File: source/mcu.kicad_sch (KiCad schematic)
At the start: 31 parts, among them J4 TYPE-C-31-M-12, P13 SWD, SW2 SW_DPDT_x2, U11 STM32F401CCU6_Blackpill, U12 STM32F401CCU6_Blackpill, U13 STM32F405RGT6, Y1 8MHz Crystal Resonator, X5032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

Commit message: jlcpcb order
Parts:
- U14: renamed from U13; LCSC (none) -> C15742
- renumbered C61 to C72, C62 to C73, C63 to C74, C64 to C75, C65 to C76, C66 to C77, C67 to C78, C68 to C79, C69 to C80, C70 to C81, C71 to C82, C72 to C83, C73 to C84, C74 to C85, R60 to R62, R61 to R63, R62 to R64, R63 to R65, R64 to R66, U11 to U12, U12 to U13
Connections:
- net PA7: now reaches U13.16 (PB2)
- net PA7: now also U14.23 (PA7(ADC12_IN7))
- net PA6: now reaches U13.17 (PB10)
- net PA6: now also U14.22 (PA6(ADC12_IN6))
- net PA4: now reaches U13.28 (PA11)
- net PA4: now also U14.20 (PA4(ADC12_IN4/DAC1_OUT))
- net PA5: now reaches U13.29 (PA12)
- net PA5: now also U14.21 (PA5(ADC12_IN5/DAC2_OUT))
- net PC4: now reaches U13.30 (PA15)
- net PC4: now also U14.24 (PC4(ADC12_IN14))
- net PC5: now reaches U13.31 (PB3)
- net PC5: now also U14.25 (PC5(ADC12_IN15))
- net PD2: now reaches U13.32 (PB4)
- net PD2: now also U14.54 (PD2)
- net PB3: now reaches U13.33 (PB5)
- net PB3: now also U14.55 (PB3(JTDO/TRACESWO))
- net PB4: now reaches U13.34 (PB6)
- net PB4: now also U14.56 (PB4(NJTRST))
- net PB12: now reaches U13.35 (PB7)
- net PB12: now also U14.33 (PB12)
- net PB2: now reaches U14.28 (PB2-BOOT1)
- net PA15: now reaches U14.50 (PA15(JTDI))
- no-connect marks 52 -> 30

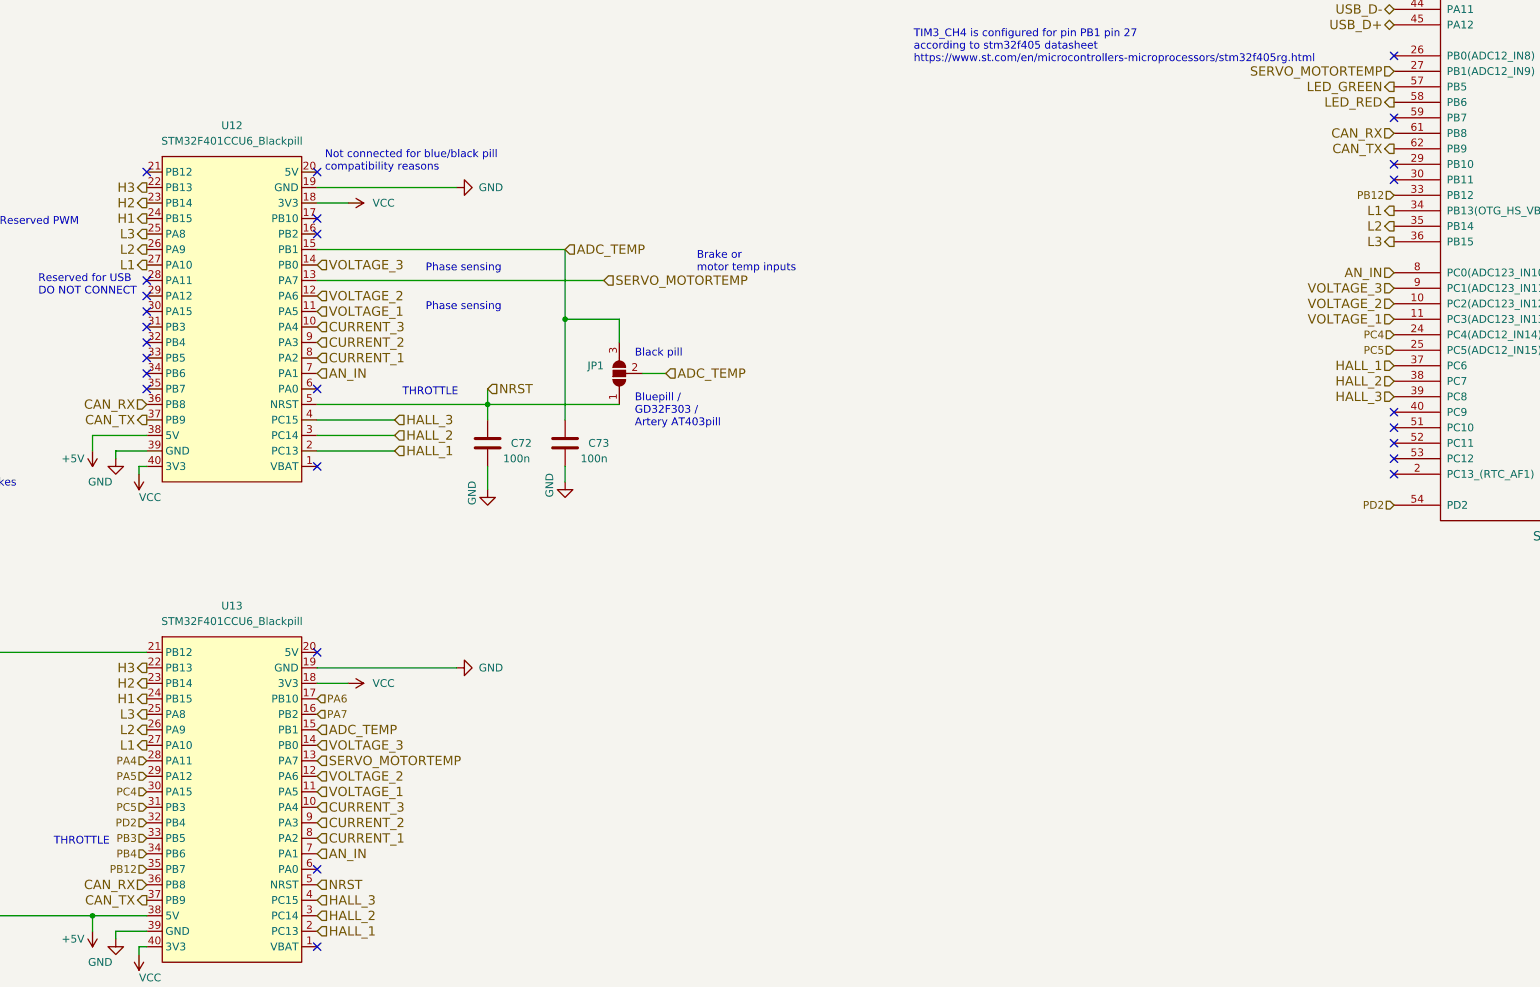
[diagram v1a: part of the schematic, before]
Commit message: Add files via upload
Bugs in the jlcbpcb order, so it was cancelled. This commit marks a new jlcpcb order.
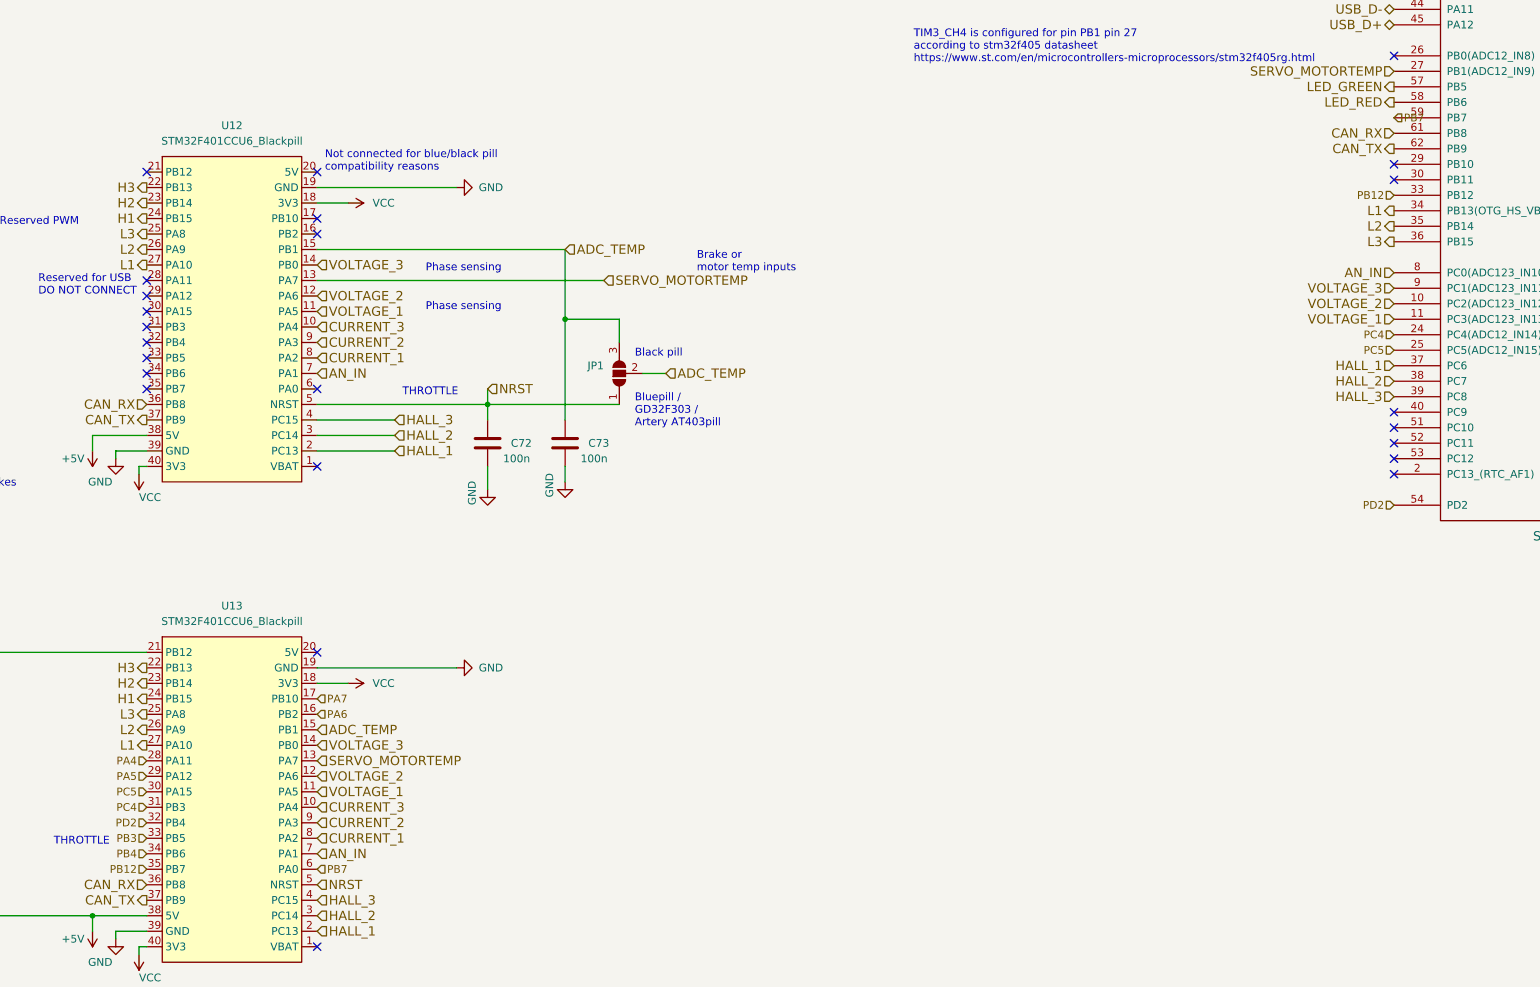
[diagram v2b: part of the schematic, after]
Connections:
- net PA6: now also U13.16 (PB2); no longer U13.17 (PB10)
- net PA7: now also U13.17 (PB10); no longer U13.16 (PB2)
- net PC4: now also U13.31 (PB3); no longer U13.30 (PA15)
- net PC5: now also U13.30 (PA15); no longer U13.31 (PB3)
- net PB7: now reaches U13.6 (PA0)
- net PB7: now also U14.59 (PB7)
- no-connect marks 30 -> 28
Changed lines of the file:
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@@
   )
   (no_connect (at 93.98 76.2))
-  (no_connect (at -82.55 209.55))
   (no_connect (at 157.48 40.64))
   (no_connect (at 157.48 43.18))
@@
   (no_connect (at 93.98 96.52))
   (no_connect (at -82.55 95.25))
-  (no_connect (at 93.98 86.36))
   (no_connect (at -110.49 130.81))
   (no_connect (at 93.98 93.98))
@@
     (effects (font (size 1.524 1.524)) (justify right))
   )
-  (hierarchical_label "PA7" (shape input) (at -82.55 184.15 0)
+  (hierarchical_label "PA7" (shape input) (at -82.55 181.61 0)
     (effects (font (size 1.27 1.27)) (justify left))
   )
@@
     (effects (font (size 1.524 1.524)) (justify right))
   )
+  (hierarchical_label "PB7" (shape input) (at -82.55 209.55 0)
+    (effects (font (size 1.27 1.27)) (justify left))
+  )
   (hierarchical_label "L2" (shape output) (at 93.98 104.14 180)
     (effects (font (size 1.524 1.524)) (justify right))
   )
-  (hierarchical_label "PC4" (shape input) (at -110.49 196.85 180)
+  (hierarchical_label "PC4" (shape input) (at -110.49 199.39 180)
     (effects (font (size 1.27 1.27)) (justify right))
   )
@@
     (effects (font (size 1.27 1.27)) (justify right))
   )
-  (hierarchical_label "PA6" (shape input) (at -82.55 181.61 0)
+  (hierarchical_label "PA6" (shape input) (at -82.55 184.15 0)
     (effects (font (size 1.27 1.27)) (justify left))
   )
@@
     (effects (font (size 1.524 1.524)) (justify right))
   )
-  (hierarchical_label "PC5" (shape input) (at -110.49 199.39 180)
+  (hierarchical_label "PC5" (shape input) (at -110.49 196.85 180)
     (effects (font (size 1.27 1.27)) (justify right))
   )
+  (hierarchical_label "PB7" (shape input) (at 93.98 86.36 0)
+    (effects (font (size 1.27 1.27)) (justify left))
+  )
   (hierarchical_label "CAN_RX" (shape input) (at -110.49 133.35 180)

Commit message: jlcpcb reorder of main-module only
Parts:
- added D9: YEL, LED_SMD:LED_0603_1608Metric, symbol Device:LED_Small
- added P11: NRF24, Connector_PinHeader_2.54mm:PinHeader_2x04_P2.54mm_Vertical, symbol Connector_Generic:Conn_02x04_Odd_Even
- added R74: 10k, Resistor_SMD:R_0603_1608Metric, symbol Device:R_Small
- renumbered D15 to D10, D16 to D11, D17 to D12, P13 to P12, R62 to R75, R63 to R76, R64 to R77, R65 to R78, R66 to R79, SW2 to SW3
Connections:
- net GND: now also P11.1 (Pin_1), R74.1
- net VCC: now also P11.2 (Pin_2)
- net at U12.32 (PB4): now also P11.7 (Pin_7)
- net at U12.33 (PB5): now also P11.6 (Pin_6)
- net at U12.34 (PB6): now also P11.5 (Pin_5)
- net at U12.35 (PB7): now also P11.4 (Pin_4)
- net at U12.6 (PA0): now also D9.2 (A), P11.3 (Pin_3)
- new net: D9.1 (K), R74.2
- no-connect marks 28 -> 24

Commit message: Add files via upload
Added six pull down resistors to mosfet gates, and removed 100 pF filter caps on current samplings. Changed Logo back to FOC-king. This is a potential release candidates - everything works, also HFI. Have not yet verified NRF though.
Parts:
- renumbered C72 to C69, C73 to C70, C74 to C71, C75 to C72, C76 to C73, C77 to C74, C78 to C75, C79 to C76, C80 to C77, C81 to C78, C82 to C79, C83 to C80, C84 to C81, C85 to C82, D9 to D10, D10 to D11, D11 to D12, D12 to D13, J4 to J5, R74 to R81, R75 to R82, R76 to R83, R77 to R84, R78 to R85, R79 to R86
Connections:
- net PC5: no longer U14.25 (PC5(ADC12_IN15))
- net AUX_ENABLE: now reaches U12.30 (PA15)
- net AUX_ENABLE: now also U14.25 (PC5(ADC12_IN15))
- no-connect marks 24 -> 23

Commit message: Moved traces to make peripherals work
PPM now works -> moved trace to PB7
UART works -> connected PB10 and PB11 to Communication port (like vesc 75_300 UART)
Removed NRF24 pinheader
Added motor_temperature to Hall pinheader, like it should be
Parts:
- removed D10: YEL, LED_SMD:LED_0603_1608Metric, symbol Device:LED_Small
- removed P11: NRF24, Connector_PinHeader_2.54mm:PinHeader_2x04_P2.54mm_Vertical, symbol Connector_Generic:Conn_02x04_Odd_Even
- removed R81: 10k, Resistor_SMD:R_0603_1608Metric, symbol Device:R_Small
- JP1: footprint Jumper:SolderJumper-3_P1.3mm_Open_RoundedPad1.0x1.5mm_NumberLabels -> Jumper:SolderJumper-3_P1.3mm_Bridged12_Pad1.0x1.5mm_NumberLabels
- renumbered D11 to D10, D12 to D11, D13 to D12, P12 to P11, R82 to R81, R83 to R82, R84 to R83, R85 to R84, R86 to R85
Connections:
- net PC5 is gone; now on net SCK_ADC_EXT: U13.30 (PA15)
- net +5V: no longer U13.21 (PB12)
- net ADC_TEMP: now also JP1.1 (A); no longer JP1.3 (B)
- net AN_IN: now also U12.14 (PB0), U13.14 (PB0); no longer U12.7 (PA1), U13.7 (PA1)
- net AUX_ENABLE: now also U12.21 (PB12), U13.21 (PB12), U14.53 (PC12); no longer U12.30 (PA15), U14.25 (PC5(ADC12_IN15))
- net NRST: now also JP1.3 (B); no longer JP1.1 (A)
- net VOLTAGE_3: now also U12.13 (PA7), U13.13 (PA7); no longer U12.14 (PB0), U13.14 (PB0)
- net PC13: now reaches U12.6 (PA0)
- net PC13: now also U13.6 (PA0), U14.2 (PC13_(RTC_AF1))
- net TEMP_MOTOR: now reaches U12.35 (PB7)
- net TEMP_MOTOR: now also U13.35 (PB7), U14.24 (PC4(ADC12_IN14))
- net ADC_15: now reaches U12.34 (PB6)
- net ADC_15: now also U13.34 (PB6), U14.25 (PC5(ADC12_IN15))
- net ADC_8: now reaches U12.33 (PB5)
- net ADC_8: now also U13.33 (PB5), U14.26 (PB0(ADC12_IN8))
- net ADC_9: now reaches U12.32 (PB4)
- net ADC_9: now also U13.32 (PB4), U14.27 (PB1(ADC12_IN9))
- net TX_SCL_MOSI: now reaches U14.29 (PB10)
- net TX_SCL_MOSI: now also U12.28 (PA11), U13.28 (PA11), U14.23 (PA7(ADC12_IN7))
- net PC14: now reaches U14.3 (PC14-OSC32_IN)
- net PC14: now also U12.7 (PA1), U13.7 (PA1)
- net RX_SDA_NSS: now reaches U14.30 (PB11)
- net RX_SDA_NSS: now also U12.31 (PB3), U13.31 (PB3), U14.20 (PA4(ADC12_IN4/DAC1_OUT))
- net SERVO: now reaches U12.17 (PB10)
- net SERVO: now also U13.17 (PB10), U14.59 (PB7)
- net MISO_ADC_EXT2: now reaches U12.29 (PA12)
- net MISO_ADC_EXT2: now also U13.29 (PA12), U14.22 (PA6(ADC12_IN6))
- removed net PA4: U13.28 (PA11), U14.20 (PA4(ADC12_IN4/DAC1_OUT))
- net PA5 renamed SCK_ADC_EXT
- net SCK_ADC_EXT: now also U12.30 (PA15); no longer U13.29 (PA12)
- net PA6: no longer names the net of U13.16 (PB2)
- net PA6: no longer U14.22 (PA6(ADC12_IN6))
- removed net PA7: U13.17 (PB10), U14.23 (PA7(ADC12_IN7))
- net PB12: no longer names the net of U14.33 (PB12)
- net PB12: no longer U13.35 (PB7)
- net PB3: no longer names the net of U14.55 (PB3(JTDO/TRACESWO))
- net PB3: no longer U13.33 (PB5)
- net PB4: no longer names the net of U14.56 (PB4(NJTRST))
- net PB4: no longer U13.34 (PB6)
- removed net PB7: U13.6 (PA0), U14.59 (PB7)
- removed net PC4: U13.31 (PB3), U14.24 (PC4(ADC12_IN14))
- net PD2: no longer names the net of U14.54 (PD2)
- net PD2: no longer U13.32 (PB4)
- removed net SERVO_MOTORTEMP: U12.13 (PA7), U13.13 (PA7), U14.27 (PB1(ADC12_IN9))
- no-connect marks 23 -> 16
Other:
- note removed: "THROTTLE"

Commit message: Add files via upload
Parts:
- removed JP1: SolderJumper_3_Open, Jumper:SolderJumper-3_P1.3mm_Bridged12_Pad1.0x1.5mm_NumberLabels, symbol Jumper:SolderJumper_3_Open
- renumbered J5 to J7
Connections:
- net +5V: now also U12.20 (5V), U13.20 (5V)
- no-connect marks 16 -> 14
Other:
- note added: "not Bluepill / GD32F303 / Artery AT403pill"
- note removed: "Black pill"
- note removed: "Bluepill / GD32F303 / Artery AT403pill"
- note removed: "Brake or motor temp inputs"
- note removed: "Not connected for blue/black pill compatibility reasons"
- moved on the sheet: C69, C70

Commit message: Momentary switch
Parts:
- added C63: 100n, Capacitor_SMD:C_0603_1608Metric, symbol Device:C
- added J6: servo, Connector_JST:JST_XH_B4B-XH-A_1x04_P2.50mm_Vertical, symbol Connector_Generic:Conn_01x04
- added R85: 100R, Resistor_SMD:R_0603_1608Metric, symbol Device:R_Small
- D10: renamed from D11; value GRN -> YEL; footprint LED_SMD:LED_0603_1608Metric -> LED_SMD:LED_0805_2012Metric; LCSC C72043 -> C2296
- D11: renamed from D12; value BLU -> WHT; LCSC C72041 -> C2290
- D9: renamed from D10; footprint LED_SMD:LED_0603_1608Metric -> LED_SMD:LED_0805_2012Metric; LCSC C2286 -> C84256
- renumbered C69 to C61, C70 to C62, C71 to C64, C72 to C65, C73 to C66, C74 to C67, C75 to C68, C76 to C69, C77 to C70, C78 to C71, C79 to C72, C80 to C73, C81 to C74, C82 to C75, R81 to R86, R82 to R87, R83 to R88, R84 to R89, R85 to R90
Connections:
- net +5V: now also J6.4 (Pin_4)
- net AUX_ENABLE: no longer U12.21 (PB12), U13.21 (PB12), U14.53 (PC12)
- net CURRENT_1: now also U12.10 (PA4), U13.10 (PA4); no longer U12.8 (PA2), U13.8 (PA2)
- net CURRENT_3: now also U12.8 (PA2), U13.8 (PA2); no longer U12.10 (PA4), U13.10 (PA4)
- net GND: now also C63.2, J6.3 (Pin_3)
- net H1: now also U12.22 (PB13), U13.22 (PB13); no longer U12.24 (PB15), U13.24 (PB15)
- net H3: now also U12.24 (PB15), U13.24 (PB15); no longer U12.22 (PB13), U13.22 (PB13)
- net HALL_1: now also U14.39 (PC8); no longer U14.37 (PC6)
- net HALL_3: now also U14.37 (PC6); no longer U14.39 (PC8)
- net L1: now also U12.25 (PA8), U13.25 (PA8); no longer U12.27 (PA10), U13.27 (PA10)
- net L3: now also U12.27 (PA10), U13.27 (PA10); no longer U12.25 (PA8), U13.25 (PA8)
- net LED_RED: now also U12.34 (PB6), U13.34 (PB6)
- net SERVO: now also U12.16 (PB2), U13.16 (PB2), C63.1, R85.2; no longer U12.17 (PB10), U13.17 (PB10)
- net VCC: now also J6.2 (Pin_2)
- net VOLTAGE_1: now also U12.13 (PA7), U13.13 (PA7); no longer U12.11 (PA5), U13.11 (PA5)
- net VOLTAGE_3: now also U12.11 (PA5), U13.11 (PA5); no longer U12.13 (PA7), U13.13 (PA7)
- removed net ADC_15: U12.34 (PB6), U13.34 (PB6), U14.25 (PC5(ADC12_IN15))
- new net: J6.1 (Pin_1), R85.1, U12.17 (PB10)
- new net PC12: U12.21 (PB12), U13.21 (PB12), U14.53 (PC12)
